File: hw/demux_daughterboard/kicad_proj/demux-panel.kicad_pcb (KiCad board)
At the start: 2 copper layers, 211.5 x 76.2 mm, 28 parts, among them P1 CONN_2, P10 CONN_2, P2 CONN_8X2, P3 CONN_8X2, P4 CONN_3X2, P5 CONN_5X2, P6 CONN_5X2, P7 CONN_2, P8 CONN_8X2, P9 CONN_8X2

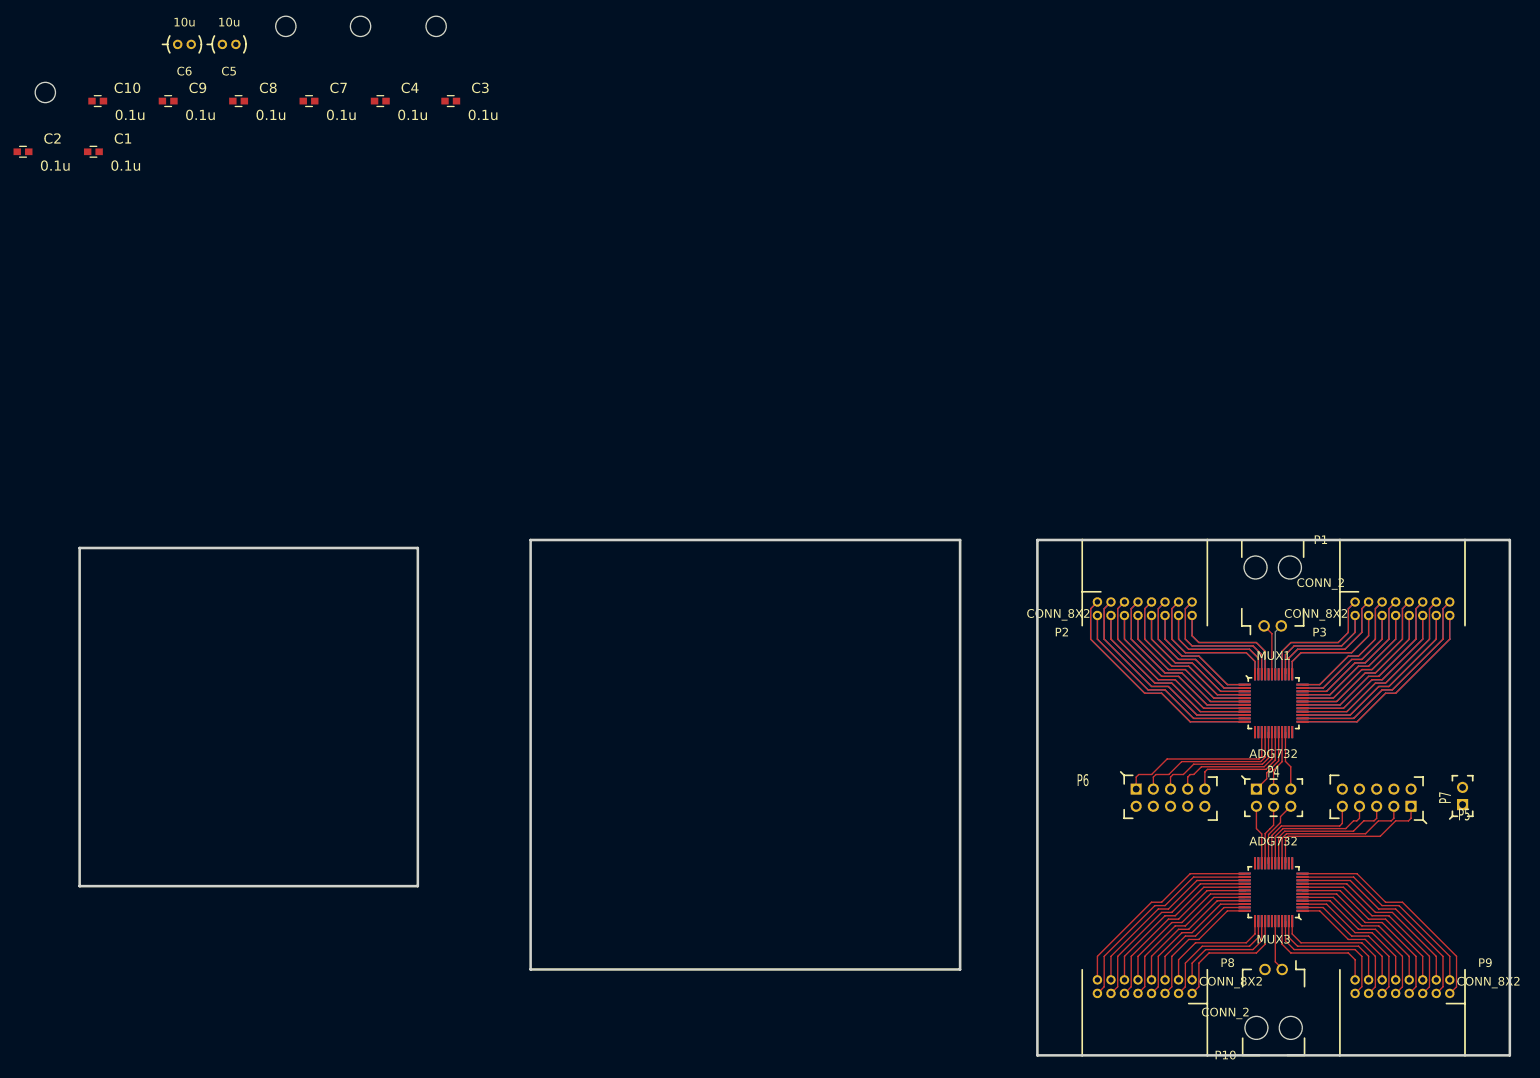
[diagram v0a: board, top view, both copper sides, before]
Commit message: Finished daughterboard pcb with fusion pcb constraints, TODO: silkscreen
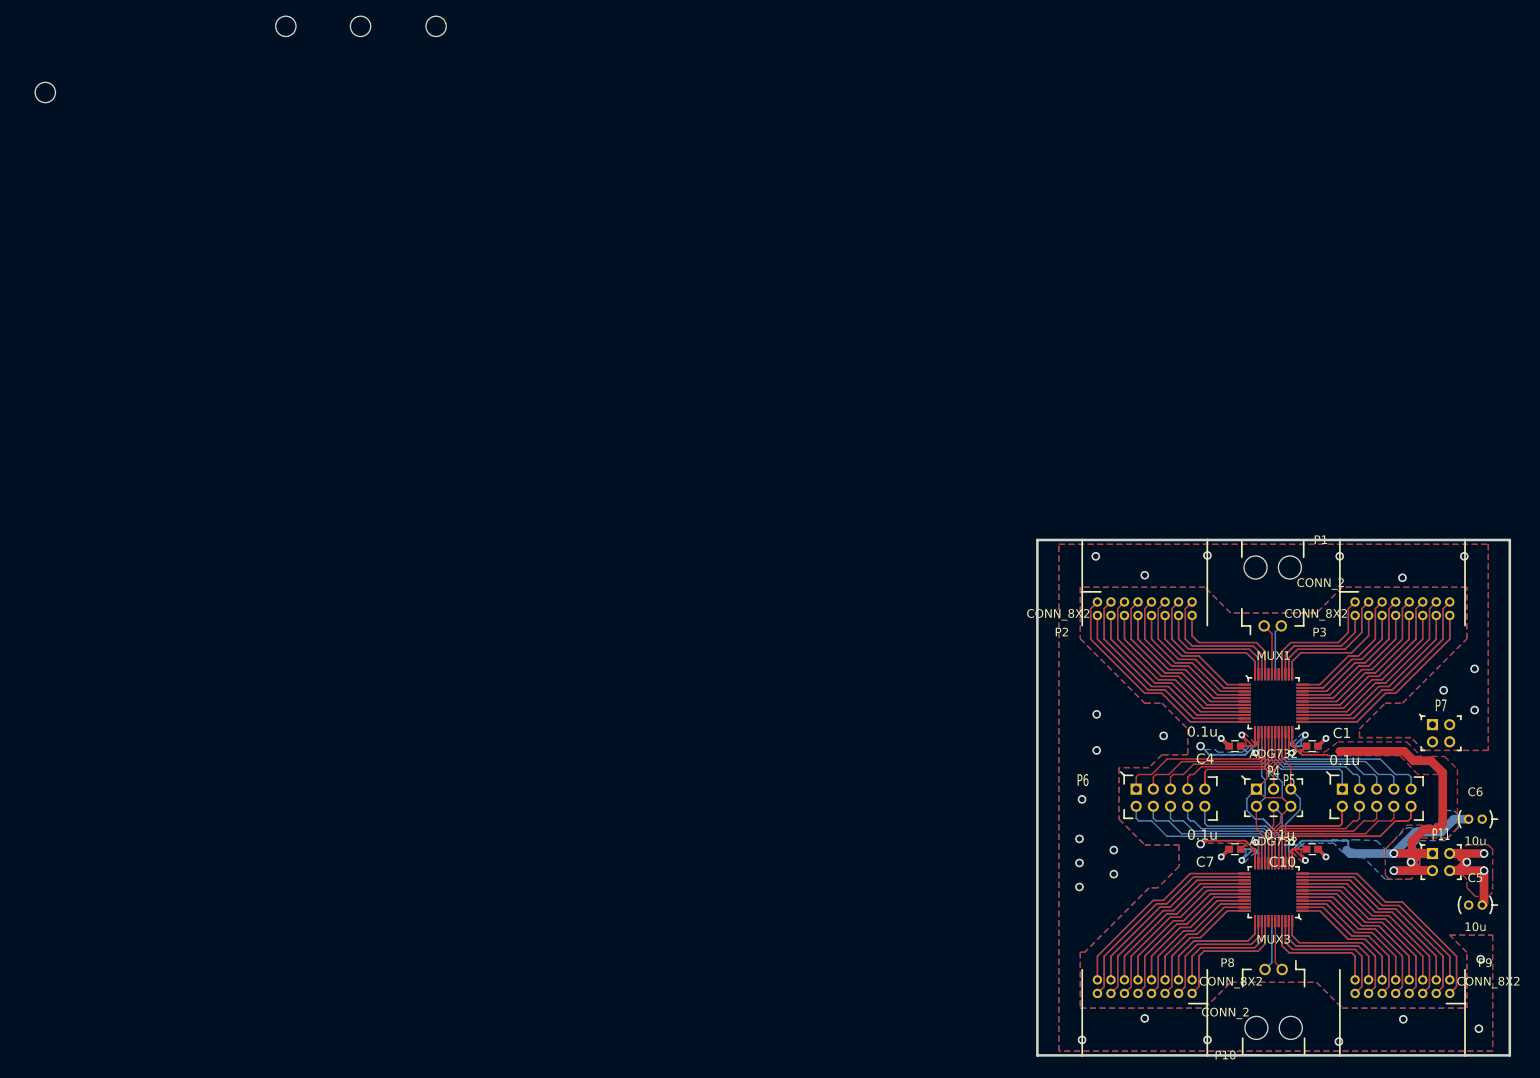
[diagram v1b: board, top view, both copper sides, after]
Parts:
- added P11: CONN_2X2, HEADER-2x2-SAMTEC, F.Cu at (241.3, 131.4)
- C2, C3, C8, C9: moved to B.Cu
- P7: value CONN_2 -> CONN_2X2; footprint HEADER-1x2-SAMTEC -> HEADER-2x2-SAMTEC
- moved C5 223.9 mm to (246.4, 137.8), turned to 180 degrees
- moved C6 222.6 mm to (246.4, 125.1), turned to 180 degrees
- moved C10 210.9 mm to (222.2, 129.5), turned to 180 degrees
- moved C1 200.5 mm to (222.2, 114.3)
- moved C2 199.6 mm to (210.8, 114.3), turned to 180 degrees
- moved C8 193.5 mm to (222.2, 129.5)
- moved C9 192.7 mm to (210.8, 129.5), turned to 180 degrees
- moved C7 176.0 mm to (210.8, 129.5), turned to 180 degrees
- moved C3 159.1 mm to (222.2, 114.3)
- moved C4 158.3 mm to (210.8, 114.3), turned to 180 degrees
- moved P7 10.0 mm to (241.3, 112.4), turned to 0 degrees
- turned P5 to 0 degrees
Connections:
- P5 pad 1: /A0 -> /B4
- P5 pad 10: /B4 -> /A0
- P5 pad 2: /B0 -> /A4
- P5 pad 3: /A1 -> /B3
- P5 pad 4: /B1 -> /A3
- P5 pad 5: /A2 -> /B2
- P5 pad 6: /B2 -> /A2
- P5 pad 7: /A3 -> /B1
- P5 pad 8: /B3 -> /A1
- P5 pad 9: /A4 -> /B0
- P7 pad 1: VDD -> GND
- P7 pad 2: VSS -> GND
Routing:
- net VSS: track 0.00 -> 173.3 mm, vias 0 -> 5
- net VDD: track 0.00 -> 61.4 mm, vias 0 -> 7
- net /B0: track 0.00 -> 50.4 mm
- net /B1: track 0.00 -> 46.5 mm
- net /B2: track 0.00 -> 42.5 mm
- net /B3: track 0.00 -> 38.6 mm
- net /CS: track 19.6 -> 55.4 mm
- net /B4: track 0.00 -> 35.6 mm
- net /OUTB1: track 33.8 -> 67.5 mm
- net /OUTB31: track 31.5 -> 63.1 mm
- net /OUTB3: track 31.3 -> 62.7 mm
- net /OUTB32: track 30.3 -> 60.7 mm
- net /OUTB2: track 30.1 -> 60.3 mm
- net /OUTB29: track 29.1 -> 58.3 mm
- net /OUTB5: track 28.9 -> 57.8 mm
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- added copper zone on B.Cu, net GND
- added copper zone on F.Cu, net GND
- added copper zone on GND, net GND
- added copper zone on B.Cu, net VDD
- added copper zone on F.Cu, net VDD
- added copper zone on PWR, net VDD
- added copper zone on B.Cu, net VSS
- added copper zone on F.Cu, net VSS
- added copper zone on PWR, net VSS
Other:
- board size 211.5 x 76.2 mm -> 69.8 x 76.2 mm
- copper layers 2 -> 4
- net class Default: via_drill 0.635 -> 0.8128
- net class Logic: via_drill 0.635 -> 0.8128
- net class Power: via_dia 0.889 -> 1.27; via_drill 0.635 -> 0.8128
- net class Signal: via_drill 0.635 -> 0.8128
- rule via_min_drill: 0.508 -> 0.3048
- rule via_min_size: 0.889 -> 0.8128

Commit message: Converting keepnote notes to thorough design documentation, starting with BRD1
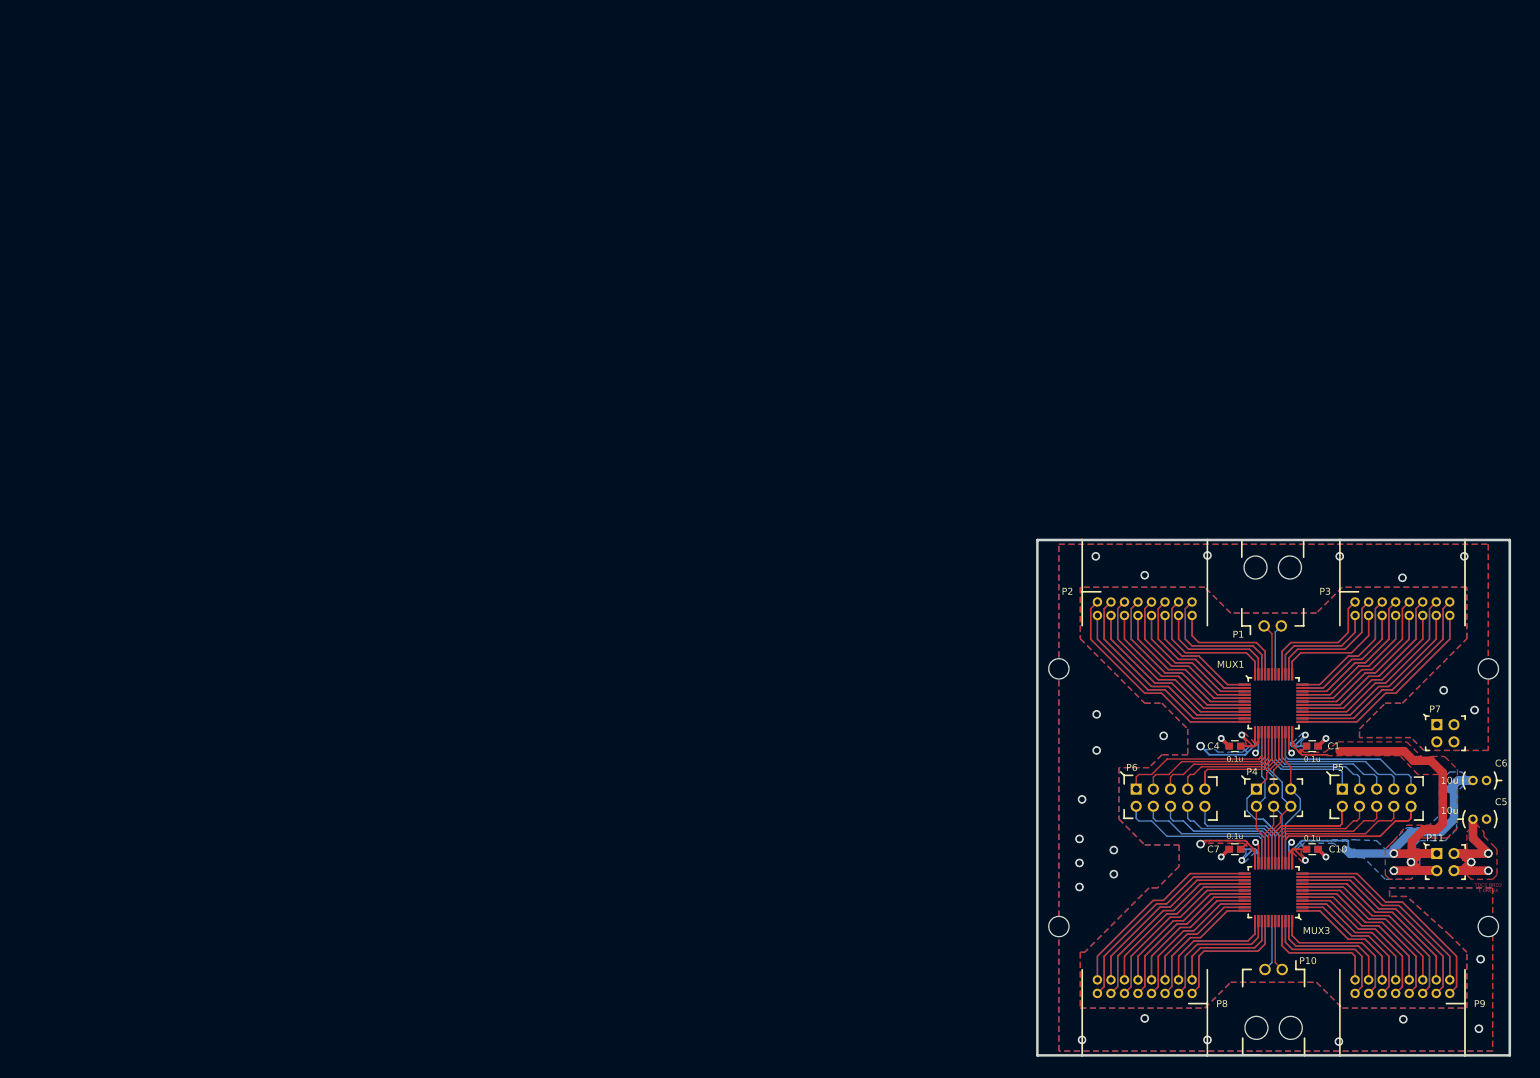
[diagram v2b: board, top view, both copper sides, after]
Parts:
- moved SCREW4 246.4 mm to (248.3, 141.0)
- moved SCREW3 182.3 mm to (248.3, 102.9)
- moved SCREW2 168.4 mm to (184.8, 141.0)
- moved SCREW1 148.6 mm to (184.8, 102.9)
- moved C5 12.7 mm to (247.0, 125.1), turned to 0 degrees
- moved C6 5.75 mm to (247.0, 119.4)
- moved P11 0.63 mm to (241.9, 131.4)
- moved P7 0.63 mm to (241.9, 112.4)
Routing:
- net VSS: track 173.3 -> 179.6 mm
- net /CS: track 55.4 -> 49.3 mm
- net VDD: track 61.4 -> 62.2 mm
- net (no net): vias 25 -> 24
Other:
- board text added: "(C) 2014 ANDREY SHMAKOV"
- board text added: "TDCS BRD2 1.0REVA"
